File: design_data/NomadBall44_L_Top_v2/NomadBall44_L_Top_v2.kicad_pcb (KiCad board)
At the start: 2 copper layers, 149 x 96.5 mm, 57 parts, among them SW1 SW_Push, SW10 SW_Push, SW11 SW_Push, SW12 SW_Push, SW13 SW_Push, SW14 SW_Push, SW15 SW_Push, SW16 SW_Push, SW17 SW_Push, SW18 SW_Push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

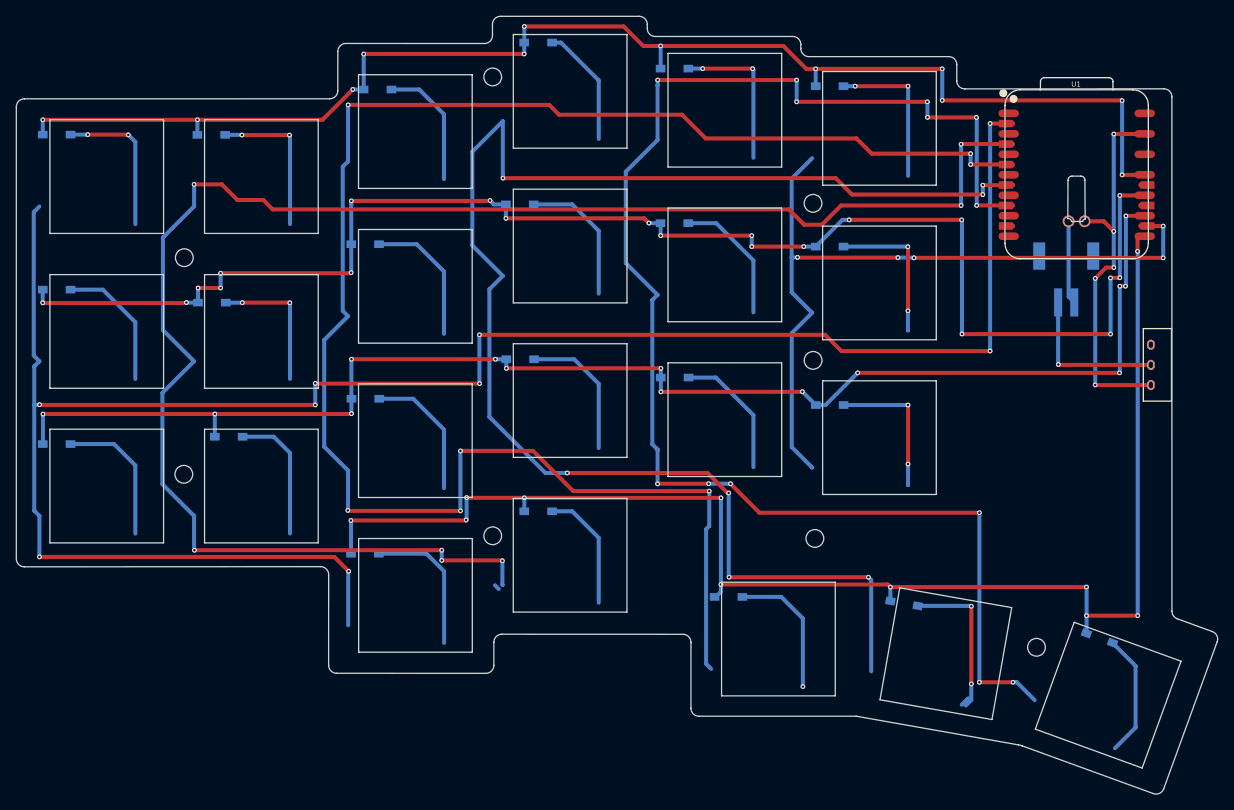
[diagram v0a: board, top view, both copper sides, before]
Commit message: 不要なフットプリントと配線を削除
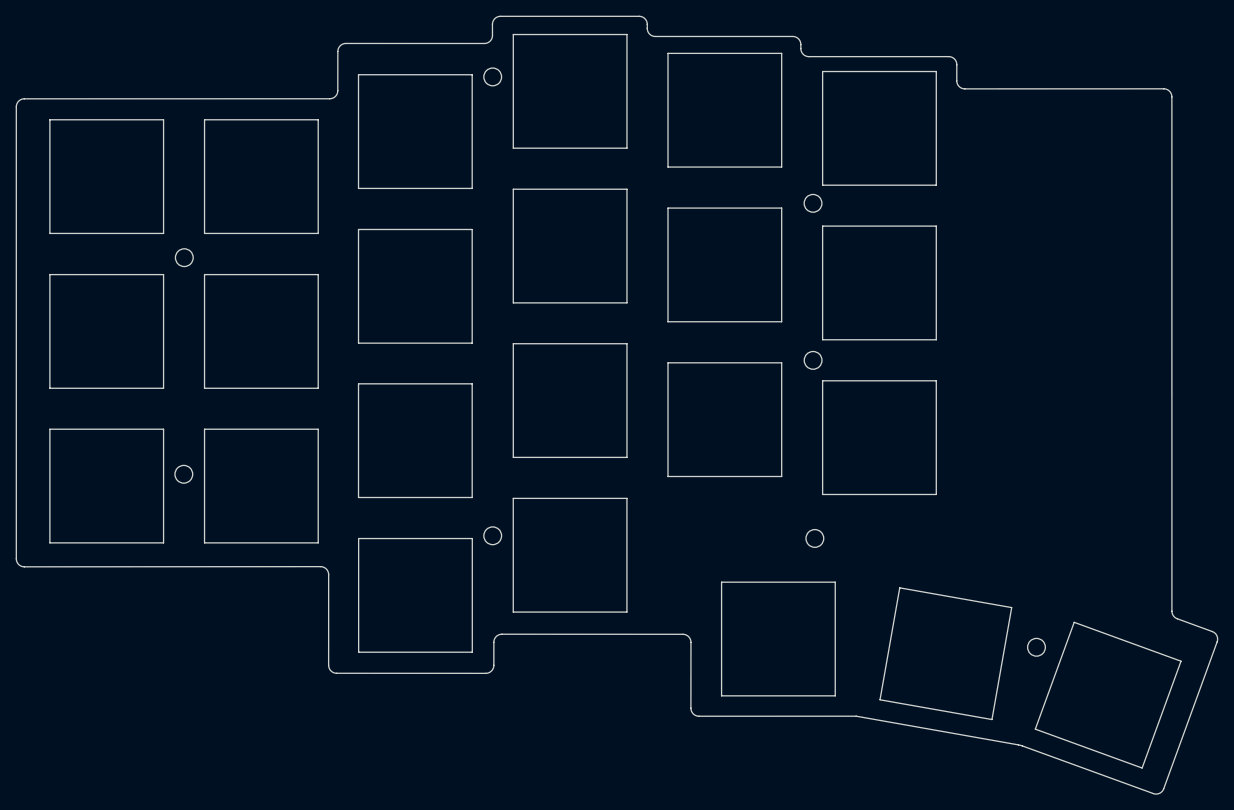
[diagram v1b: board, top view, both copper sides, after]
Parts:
- removed BT1: Battery_Cell, NomadBall44:JST_S2B-PH-SM4-TB
- removed D1, D10, D11, D12, D13, D14, D15, D16, D17, D18, D19, D2, D20, D21, D22, D23, D3, D4, D5, D6, D7, D8, D9: D, NomadBall44:Diode_SMD
- removed SW24: SW_SPDT, NomadBall44:TGSW_MSK-12D19
- removed U1: XIAO-nRF52840-Plus-SMD, NomadBall44:XIAO-nRF52840-Plus-ver3
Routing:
- net Col0: track 248.9 -> 0.00 mm, vias 9 -> 0
- net Col2: track 215.7 -> 0.00 mm, vias 7 -> 0
- net Col1: track 206.5 -> 0.00 mm, vias 7 -> 0
- net Row1: track 188.0 -> 0.00 mm, vias 21 -> 0
- net Col3: track 185.3 -> 0.00 mm, vias 7 -> 0
- net Col4: track 183.0 -> 0.00 mm, vias 13 -> 0
- net Row2: track 175.0 -> 0.00 mm, vias 14 -> 0
- net Row3: track 173.7 -> 0.00 mm, vias 11 -> 0
- net Row0: track 169.2 -> 0.00 mm, vias 12 -> 0
- net Col5: track 94.7 -> 0.00 mm, vias 5 -> 0
- net GND: track 46.7 -> 0.00 mm, vias 5 -> 0
- net Net-(D22-A): track 20.4 -> 0.00 mm, vias 2 -> 0
- net Net-(BT1--): track 19.2 -> 0.00 mm, vias 1 -> 0
- net Net-(D6-A): track 19.1 -> 0.00 mm, vias 2 -> 0
- net Net-(D2-A): track 19.1 -> 0.00 mm, vias 2 -> 0
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
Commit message: 左手トッププレート完成
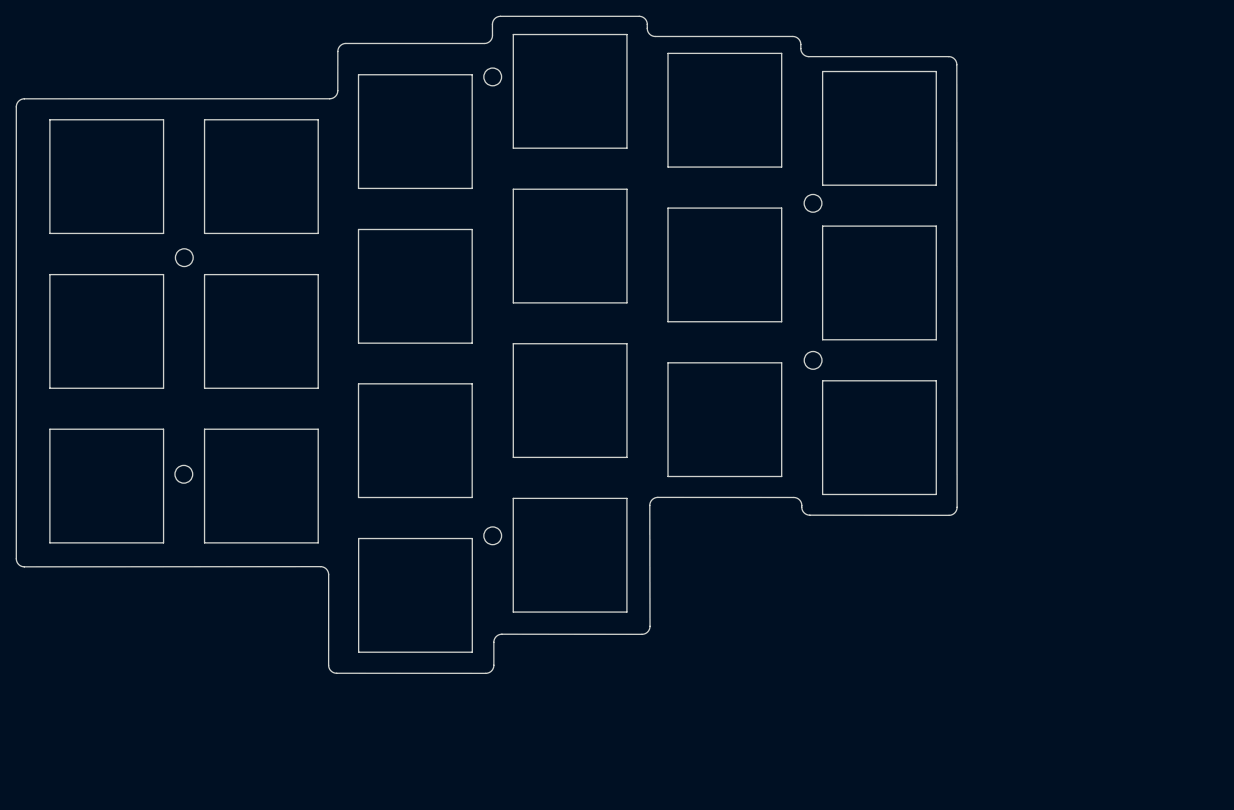
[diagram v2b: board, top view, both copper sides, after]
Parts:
- removed the REF** at (230.9, 119.9)
- removed the REF** at (258.4, 133.4)
- removed SW21, SW22, SW23: SW_Push, NomadBall44:SW_Hole_1u
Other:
- board size 149 x 96.5 mm -> 116.7 x 81.5 mm
